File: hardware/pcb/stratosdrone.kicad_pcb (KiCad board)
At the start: 4 copper layers, 38 x 74 mm, 115 parts, among them J1 BATT_PH2, J10 DBG, J11 C6DBG, J2 USB-C-16P, J3 FLOW_HDR, J4 CAM_FFC15, J5 MOTOR1, J6 MOTOR2, J7 MOTOR3, J8 MOTOR4, J9 EXP, Q1 AO3400A, Q2 AO3400A, Q3 AO3400A, Q4 AO3400A, SW1 RESET, SW2 BOOT, U1 ESP32-P4NRW32, U10 TLV62569DBVR, U2 W25Q128JVSIQ, U3 ESP32-C6-MINI-1, U4 TP4056-42-ESOP8, U5 SY8089AAAC, U6 ICM-42688-P, U7 SPL06-001, U8 VL53L1X, U9 PMW3901MB, Y1 40MHz

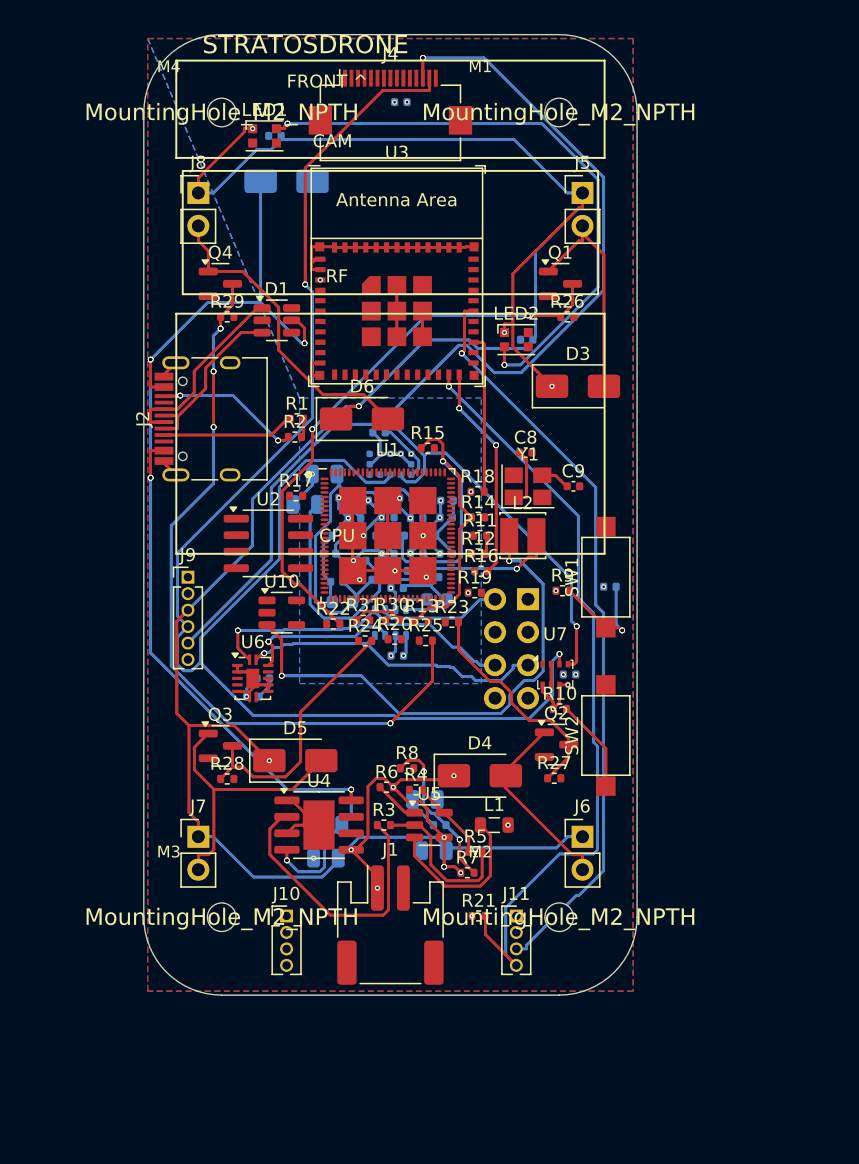
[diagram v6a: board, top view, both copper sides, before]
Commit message: pcb: add 51 clearance-checked power stitch vias; document the true routing gap
Verification pass on the PCB (placement, routing, sensors, camera):

- Ran connect_power() (pure pcbnew, no autorouter) to stitch power-net pads
  not already touching their plane: +51 clearance-checked vias (172 total,
  up from 121). Re-exported gerbers + the JLCPCB zip.
- Confirmed with KiCad's own connectivity engine (not eyeballing): 106
  pad-pairs across 73 nets are still ratsnest, almost all needing just one
  more short trace/via. Full net list now in KNOWN_GAPS.md item 1.
- Verified sensor + camera placement against the frame: the ToF/flow Y
  offsets in body_bottom_v2.scad (tof_pos=[0,-3.9], flow_pos=[0,8.3]) match
  the PCB's board-center-relative positions exactly; camera FFC sits at the
  nose, matching the frame's front-wall opening.
- Identified the "8 holes" connector: J3 (FLOW_HDR), a DNP 2x4 fallback
  header for the optical-flow sensor — populate U9 (soldered PMW3901) OR
  J3 (external CJMCU-3901 breakout), not both.
- Tried 5 different headless-Freerouting configurations to close the
  remaining gap automatically; all 5 converge on the routing internally but
  never write the session file (looks like a real bug in Freerouting
  2.1.0's post-route save path under a headless X server, not a config
  issue — documented in KNOWN_GAPS/ROUTING so it isn't re-attempted blind).

Board is NOT yet ready to order: the zip in jlcpcb/ reflects the current,
mostly-but-not-fully-routed state. KNOWN_GAPS.md lists the fastest paths to
close the last ~106 connections (KiCad direct / DeepPCB.ai / Freerouting
with a real display).

Co-Authored-By: Claude Opus 4.8 <noreply@anthropic.com>
Claude-Session: https://claude.ai/code/session_011szEEHZ8KTTsZmGFgY6Cjw
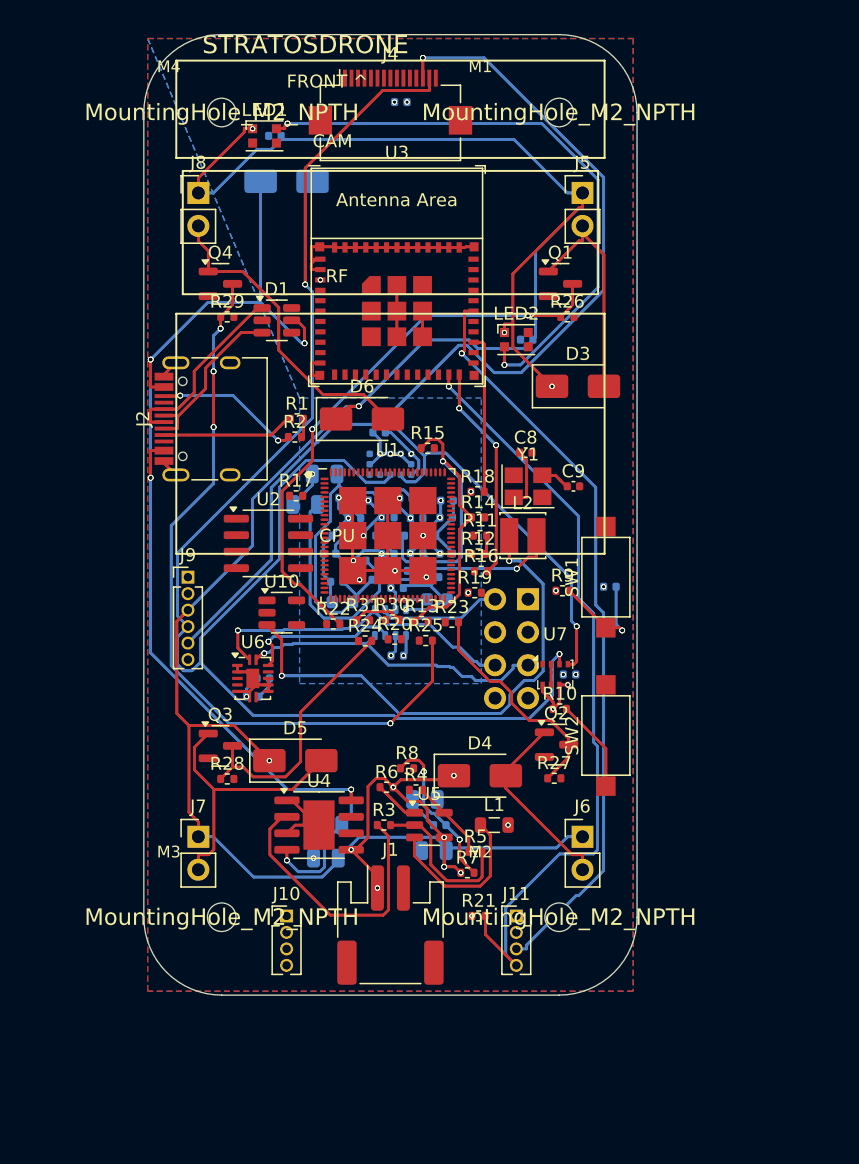
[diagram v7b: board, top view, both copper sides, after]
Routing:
- net VBAT: vias 14 -> 24
- net GND: vias 28 -> 56
- net 3V3: vias 13 -> 26
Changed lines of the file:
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@@
   (segment (start 13.55 16.35) (end 14.65 16.35) (width 0.2) (layer "F.Cu") (net 1))
   (segment (start 21.9 16.4) (end 21.1 16.4) (width 0.2) (layer "F.Cu") (net 1))
+  (via (at 21.765343 41.796811) (size 0.4) (drill 0.2) (layers "F.Cu" "B.Cu") (net 1))
   (via (at 18.32 40) (size 0.4) (drill 0.2) (layers "F.Cu" "B.Cu") (net 1))
   (via (at 19.348354 41.311547) (size 0.4) (drill 0.2) (layers "F.Cu" "B.Cu") (net 1))
   (via (at 17.291645 35.888452) (size 0.4) (drill 0.2) (layers "F.Cu" "B.Cu") (net 1))
+  (via (at 20.54149 39.950918) (size 0.4) (drill 0.2) (layers "F.Cu" "B.Cu") (net 1))
   (via (at 16.149318 40.523055) (size 0.4) (drill 0.2) (layers "F.Cu" "B.Cu") (net 1))
   (via (at 7.92 51) (size 0.4) (drill 0.2) (layers "F.Cu" "B.Cu") (net 1))
   (via (at 22.811192 37.21465) (size 0.4) (drill 0.2) (layers "F.Cu" "B.Cu") (net 1))
+  (via (at 7.92 51) (size 0.4) (drill 0.2) (layers "F.Cu" "B.Cu") (net 1))
   (via (at 15.752177 37.252302) (size 0.4) (drill 0.2) (layers "F.Cu" "B.Cu") (net 1))
+  (via (at 15.752177 37.252302) (size 0.4) (drill 0.2) (layers "F.Cu" "B.Cu") (net 1))
+  (via (at 12.980165 33.853979) (size 0.4) (drill 0.2) (layers "F.Cu" "B.Cu") (net 1))
   (via (at 19.32 5.2) (size 0.4) (drill 0.2) (layers "F.Cu" "B.Cu") (net 1))
+  (via (at 18.2 32.3) (size 0.4) (drill 0.2) (layers "F.Cu" "B.Cu") (net 1))
+  (via (at 19.8 32.3) (size 0.4) (drill 0.2) (layers "F.Cu" "B.Cu") (net 1))
+  (via (at 13.078985 63.445618) (size 0.4) (drill 0.2) (layers "F.Cu" "B.Cu") (net 1))
   (via (at 16.626194 42.00162) (size 0.4) (drill 0.2) (layers "F.Cu" "B.Cu") (net 1))
   (via (at 21.765343 41.796811) (size 0.4) (drill 0.2) (layers "F.Cu" "B.Cu") (net 1))
   (via (at 19 32.3) (size 0.4) (drill 0.2) (layers "F.Cu" "B.Cu") (net 1))
+  (via (at 17.291645 35.888452) (size 0.4) (drill 0.2) (layers "F.Cu" "B.Cu") (net 1))
+  (via (at 22.880128 35.899031) (size 0.4) (drill 0.2) (layers "F.Cu" "B.Cu") (net 1))
   (via (at 21.52 38.6) (size 0.4) (drill 0.2) (layers "F.Cu" "B.Cu") (net 1))
   (via (at 18.32 37.2) (size 0.4) (drill 0.2) (layers "F.Cu" "B.Cu") (net 1))
   (via (at 19.8 32.3) (size 0.4) (drill 0.2) (layers "F.Cu" "B.Cu") (net 1))
+  (via (at 19.031957 42.637711) (size 0.4) (drill 0.2) (layers "F.Cu" "B.Cu") (net 1))
+  (via (at 16.626194 42.00162) (size 0.4) (drill 0.2) (layers "F.Cu" "B.Cu") (net 1))
   (via (at 20.54149 37.249081) (size 0.4) (drill 0.2) (layers "F.Cu" "B.Cu") (net 1))
+  (via (at 19.708427 35.716899) (size 0.4) (drill 0.2) (layers "F.Cu" "B.Cu") (net 1))
+  (via (at 19.348354 41.311547) (size 0.4) (drill 0.2) (layers "F.Cu" "B.Cu") (net 1))
+  (via (at 19 32.3) (size 0.4) (drill 0.2) (layers "F.Cu" "B.Cu") (net 1))
+  (via (at 16.149318 40.523055) (size 0.4) (drill 0.2) (layers "F.Cu" "B.Cu") (net 1))
   (via (at 19.048985 47.845618) (size 0.4) (drill 0.2) (layers "F.Cu" "B.Cu") (net 1))
+  (via (at 18.32 40) (size 0.4) (drill 0.2) (layers "F.Cu" "B.Cu") (net 1))
   (via (at 15.026552 35.68226) (size 0.4) (drill 0.2) (layers "F.Cu" "B.Cu") (net 1))
+  (via (at 15.026552 35.68226) (size 0.4) (drill 0.2) (layers "F.Cu" "B.Cu") (net 1))
+  (via (at 16.92 38.6) (size 0.4) (drill 0.2) (layers "F.Cu" "B.Cu") (net 1))
   (via (at 18.2 32.3) (size 0.4) (drill 0.2) (layers "F.Cu" "B.Cu") (net 1))
   (via (at 20.54149 39.950918) (size 0.4) (drill 0.2) (layers "F.Cu" "B.Cu") (net 1))
+  (via (at 21.52 38.6) (size 0.4) (drill 0.2) (layers "F.Cu" "B.Cu") (net 1))
+  (via (at 35.426146 42.539103) (size 0.4) (drill 0.2) (layers "F.Cu" "B.Cu") (net 1))
   (via (at 19.708427 35.716899) (size 0.4) (drill 0.2) (layers "F.Cu" "B.Cu") (net 1))
+  (via (at 19.32 5.2) (size 0.4) (drill 0.2) (layers "F.Cu" "B.Cu") (net 1))
   (via (at 22.880128 35.899031) (size 0.4) (drill 0.2) (layers "F.Cu" "B.Cu") (net 1))
   (via (at 19.031957 42.637711) (size 0.4) (drill 0.2) (layers "F.Cu" "B.Cu") (net 1))
+  (via (at 32.319999 49.3) (size 0.4) (drill 0.2) (layers "F.Cu" "B.Cu") (net 1))
   (via (at 35.426146 42.539103) (size 0.4) (drill 0.2) (layers "F.Cu" "B.Cu") (net 1))
+  (via (at 20.54149 37.249081) (size 0.4) (drill 0.2) (layers "F.Cu" "B.Cu") (net 1))
+  (via (at 22.811192 39.985349) (size 0.4) (drill 0.2) (layers "F.Cu" "B.Cu") (net 1))
+  (via (at 22.811192 37.21465) (size 0.4) (drill 0.2) (layers "F.Cu" "B.Cu") (net 1))
   (via (at 22.811192 39.985349) (size 0.4) (drill 0.2) (layers "F.Cu" "B.Cu") (net 1))
   (via (at 12.980165 33.853979) (size 0.4) (drill 0.2) (layers "F.Cu" "B.Cu") (net 1))
+  (via (at 18.32 37.2) (size 0.4) (drill 0.2) (layers "F.Cu" "B.Cu") (net 1))
   (via (at 16.92 38.6) (size 0.4) (drill 0.2) (layers "F.Cu" "B.Cu") (net 1))
+  (via (at 19.048985 47.845618) (size 0.4) (drill 0.2) (layers "F.Cu" "B.Cu") (net 1))
   (via (at 13.078985 63.445618) (size 0.4) (drill 0.2) (layers "F.Cu" "B.Cu") (net 1))
   (via (at 32.319999 49.3) (size 0.4) (drill 0.2) (layers "F.Cu" "B.Cu") (net 1))
@@
   (via (at 31.539295 51.95) (size 0.4) (drill 0.2) (layers "F.Cu" "B.Cu") (net 4))
   (via (at 25.289999 67.9) (size 0.4) (drill 0.2) (layers "F.Cu" "B.Cu") (net 4))
+  (via (at 20.008985 47.845618) (size 0.4) (drill 0.2) (layers "F.Cu" "B.Cu") (net 4))
+  (via (at 32.675 50.1) (size 0.4) (drill 0.2) (layers "F.Cu" "B.Cu") (net 4))
+  (via (at 31.539295 51.95) (size 0.4) (drill 0.2) (layers "F.Cu" "B.Cu") (net 4))
+  (via (at 31.750512 42.84777) (size 0.4) (drill 0.2) (layers "F.Cu" "B.Cu") (net 4))
   (via (at 25.205583 35.214042) (size 0.4) (drill 0.2) (layers "F.Cu" "B.Cu") (net 4))
   (via (at 20.28 5.2) (size 0.4) (drill 0.2) (layers "F.Cu" "B.Cu") (net 4))
   (via (at 28.0625 60.9) (size 0.4) (drill 0.2) (layers "F.Cu" "B.Cu") (net 4))
+  (via (at 20.28 5.2) (size 0.4) (drill 0.2) (layers "F.Cu" "B.Cu") (net 4))
   (via (at 33.279999 49.3) (size 0.4) (drill 0.2) (layers "F.Cu" "B.Cu") (net 4))
   (via (at 20.008985 47.845618) (size 0.4) (drill 0.2) (layers "F.Cu" "B.Cu") (net 4))
   (via (at 24.99 43) (size 0.4) (drill 0.2) (layers "F.Cu" "B.Cu") (net 4))
+  (via (at 20.6 32.3) (size 0.4) (drill 0.2) (layers "F.Cu" "B.Cu") (net 4))
+  (via (at 25.205583 35.214042) (size 0.4) (drill 0.2) (layers "F.Cu" "B.Cu") (net 4))
   (via (at 20.2 44.3) (size 0.4) (drill 0.2) (layers "F.Cu" "B.Cu") (net 4))
   (via (at 32.675 50.1) (size 0.4) (drill 0.2) (layers "F.Cu" "B.Cu") (net 4))
+  (via (at 24.99 43) (size 0.4) (drill 0.2) (layers "F.Cu" "B.Cu") (net 4))
   (via (at 31.750512 42.84777) (size 0.4) (drill 0.2) (layers "F.Cu" "B.Cu") (net 4))
+  (via (at 28.0625 60.9) (size 0.4) (drill 0.2) (layers "F.Cu" "B.Cu") (net 4))
+  (via (at 13.6 18.9) (size 0.4) (drill 0.2) (layers "F.Cu" "B.Cu") (net 4))
   (via (at 20.6 32.3) (size 0.4) (drill 0.2) (layers "F.Cu" "B.Cu") (net 4))
+  (via (at 20.2 44.3) (size 0.4) (drill 0.2) (layers "F.Cu" "B.Cu") (net 4))
+  (via (at 25.289999 67.9) (size 0.4) (drill 0.2) (layers "F.Cu" "B.Cu") (net 4))
   (via (at 13.6 18.9) (size 0.4) (drill 0.2) (layers "F.Cu" "B.Cu") (net 4))
+  (via (at 33.279999 49.3) (size 0.4) (drill 0.2) (layers "F.Cu" "B.Cu") (net 4))
   (segment (start 22.2746 44.3) (end 20.2 44.3) (width 0.2) (layer "B.Cu") (net 4))
   (segment (start 15.9866 36.5267) (end 16.7122 37.2523) (width 0.2) (layer "B.Cu") (net 4))
@@
   (segment (start 3.4769 59.925) (end 4.2 60.6481) (width 0.2) (layer "F.Cu") (net 59))
   (segment (start 4.2 61.8) (end 4.2 60.6481) (width 0.2) (layer "F.Cu") (net 59))
+  (via (at 18 65.75) (size 0.4) (drill 0.2) (layers "F.Cu" "B.Cu") (net 59))
+  (via (at 15.975 62.805) (size 0.4) (drill 0.2) (layers "F.Cu" "B.Cu") (net 59))
   (via (at 31.450705 27.095905) (size 0.4) (drill 0.2) (layers "F.Cu" "B.Cu") (net 59))
   (via (at 19.216552 57.98226) (size 0.4) (drill 0.2) (layers "F.Cu" "B.Cu") (net 59))
@@
   (via (at 16.5652 28.6318) (size 0.45) (drill 0.25) (layers "F.Cu" "B.Cu") (net 59))
   (via (at 23.1375 64.1168) (size 0.45) (drill 0.25) (layers "F.Cu" "B.Cu") (net 59))
+  (via (at 31.450705 27.095905) (size 0.4) (drill 0.2) (layers "F.Cu" "B.Cu") (net 59))
   (via (at 8.385 7.25) (size 0.4) (drill 0.2) (layers "F.Cu" "B.Cu") (net 59))
   (via (at 23.891959 57.098628) (size 0.4) (drill 0.2) (layers "F.Cu" "B.Cu") (net 59))
+  (via (at 19.216552 57.98226) (size 0.4) (drill 0.2) (layers "F.Cu" "B.Cu") (net 59))
+  (via (at 24.420402 64.574607) (size 0.4) (drill 0.2) (layers "F.Cu" "B.Cu") (net 59))
+  (via (at 27.785 22.95) (size 0.4) (drill 0.2) (layers "F.Cu" "B.Cu") (net 59))
   (via (at 9.674076 55.935856) (size 0.4) (drill 0.2) (layers "F.Cu" "B.Cu") (net 59))
+  (via (at 23.891959 57.098628) (size 0.4) (drill 0.2) (layers "F.Cu" "B.Cu") (net 59))
   (via (at 16.5652 28.6318) (size 0.45) (drill 0.25) (layers "F.Cu" "B.Cu") (net 59))
   (via (at 23.1375 64.1168) (size 0.45) (drill 0.25) (layers "F.Cu" "B.Cu") (net 59))
+  (via (at 23.1375 61.85) (size 0.4) (drill 0.2) (layers "F.Cu" "B.Cu") (net 59))
   (via (at 18 65.75) (size 0.4) (drill 0.2) (layers "F.Cu" "B.Cu") (net 59))
+  (via (at 9.674076 55.935856) (size 0.4) (drill 0.2) (layers "F.Cu" "B.Cu") (net 59))
+  (via (at 8.385 7.25) (size 0.4) (drill 0.2) (layers "F.Cu" "B.Cu") (net 59))
   (segment (start 23.2973 62.6616) (end 22.4669 61.8312) (width 0.2) (layer "B.Cu") (net 59))
   (segment (start 14.979 63.6619) (end 14.979 63.4456) (width 0.2) (layer "B.Cu") (net 59))

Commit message: hardware/pcb: add Stratos Drones S-propeller logo + wordmark to silkscreen
Recreated the "S made of two swept propeller blades around a hub" logo and
the "STRATOS DRONES" wordmark on the back silkscreen (B.SilkS), matching the
project branding. Added via scripts/add_logo.py — a text-level append that
preserves the existing routing (1384 tracks / 174 vias unchanged) and is
idempotent. The mark sits in the clean B.Cu-pour area above the sensor
aperture (y<27 mm) so it never overlaps the optical windows; the wordmark
runs along the bottom edge. Documented in KNOWN_GAPS process notes; preview
render in preview/back_silk_logo.png.

Co-Authored-By: Claude Fable 5 <noreply@anthropic.com>
Claude-Session: https://claude.ai/code/session_011szEEHZ8KTTsZmGFgY6Cjw
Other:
- board text added: "STRATOS DRONES"
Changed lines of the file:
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@@
     )
   )
+  (gr_poly (pts (xy 19.125 22.000) (xy 18.921 21.828) (xy 18.727 21.644) (xy 18.543 21.451) (xy 18.368 21.248) (xy 18.204 21.035) (xy 18.051 20.815) (xy 17.908 20.587) (xy 17.777 20.351) (xy 17.656 20.109) (xy 17.547 19.862) (xy 17.451 19.609) (xy 17.366 19.352) (xy 17.293 19.091) (xy 17.233 18.826) (xy 17.186 18.560) (xy 17.152 18.291) (xy 17.132 18.021) (xy 17.125 17.750) (xy 16.946 17.926) (xy 16.783 18.118) (xy 16.637 18.326) (xy 16.509 18.548) (xy 16.398 18.783) (xy 16.306 19.028) (xy 16.232 19.282) (xy 16.176 19.544) (xy 16.141 19.812) (xy 16.124 20.085) (xy 16.128 20.361) (xy 16.153 20.639) (xy 16.198 20.916) (xy 16.264 21.192) (xy 16.352 21.465) (xy 16.462 21.734) (xy 16.595 21.996) (xy 16.750 22.250) (xy 16.815 22.331) (xy 16.884 22.407) (xy 16.958 22.479) (xy 17.036 22.545) (xy 17.118 22.606) (xy 17.204 22.662) (xy 17.294 22.713) (xy 17.387 22.758) (xy 17.484 22.797) (xy 17.585 22.830) (xy 17.689 22.858) (xy 17.796 22.880) (xy 17.907 22.895) (xy 18.020 22.904) (xy 18.136 22.907) (xy 18.255 22.903) (xy 18.376 22.892) (xy 18.500 22.875) (xy 18.581 22.853) (xy 18.657 22.829) (xy 18.729 22.802) (xy 18.795 22.772) (xy 18.856 22.739) (xy 18.912 22.704) (xy 18.963 22.665) (xy 19.008 22.623) (xy 19.047 22.578) (xy 19.080 22.529) (xy 19.108 22.477) (xy 19.130 22.421) (xy 19.145 22.361) (xy 19.154 22.298) (xy 19.157 22.230) (xy 19.153 22.158) (xy 19.142 22.081) (xy 19.125 22.000)) (stroke (width 0) (type solid)) (fill solid) (layer "B.SilkS") (tstamp stratos-logo-ed339a43-24d2-4dee-8aad-c41e2fa42c7e))
+  (gr_poly (pts (xy 18.875 23.000) (xy 19.079 23.172) (xy 19.273 23.356) (xy 19.457 23.549) (xy 19.632 23.752) (xy 19.796 23.965) (xy 19.949 24.185) (xy 20.092 24.413) (xy 20.223 24.649) (xy 20.344 24.891) (xy 20.453 25.138) (xy 20.549 25.391) (xy 20.634 25.648) (xy 20.707 25.909) (xy 20.767 26.174) (xy 20.814 26.440) (xy 20.848 26.709) (xy 20.868 26.979) (xy 20.875 27.250) (xy 21.054 27.074) (xy 21.217 26.882) (xy 21.363 26.674) (xy 21.491 26.452) (xy 21.602 26.217) (xy 21.694 25.972) (xy 21.768 25.718) (xy 21.824 25.456) (xy 21.859 25.188) (xy 21.876 24.915) (xy 21.872 24.639) (xy 21.847 24.361) (xy 21.802 24.084) (xy 21.736 23.808) (xy 21.648 23.535) (xy 21.538 23.266) (xy 21.405 23.004) (xy 21.250 22.750) (xy 21.185 22.669) (xy 21.116 22.593) (xy 21.042 22.521) (xy 20.964 22.455) (xy 20.882 22.394) (xy 20.796 22.338) (xy 20.706 22.287) (xy 20.613 22.242) (xy 20.516 22.203) (xy 20.415 22.170) (xy 20.311 22.142) (xy 20.204 22.120) (xy 20.093 22.105) (xy 19.980 22.096) (xy 19.864 22.093) (xy 19.745 22.097) (xy 19.624 22.108) (xy 19.500 22.125) (xy 19.419 22.147) (xy 19.343 22.171) (xy 19.271 22.198) (xy 19.205 22.228) (xy 19.144 22.261) (xy 19.088 22.296) (xy 19.037 22.335) (xy 18.992 22.377) (xy 18.953 22.422) (xy 18.920 22.471) (xy 18.892 22.523) (xy 18.870 22.579) (xy 18.855 22.639) (xy 18.846 22.702) (xy 18.843 22.770) (xy 18.847 22.842) (xy 18.858 22.919) (xy 18.875 23.000)) (stroke (width 0) (type solid)) (fill solid) (layer "B.SilkS") (tstamp stratos-logo-5fa175e6-d708-49c5-ba64-9c1fbd1f2083))
+  (gr_circle (center 19.000 22.500) (end 19.938 22.500) (stroke (width 0.625) (type solid)) (fill none) (layer "B.SilkS") (tstamp stratos-logo-dd315498-a2ae-4508-9006-7bf8bd8fba50))
+  (gr_circle (center 19.000 22.500) (end 19.250 22.500) (stroke (width 0.000) (type solid)) (fill solid) (layer "B.SilkS") (tstamp stratos-logo-91948ab8-85fd-444a-baa2-42ef5cbcf667))
+  (gr_text "STRATOS DRONES" (at 19.000 68.500) (layer "B.SilkS") (effects (font (size 1.5 1.5) (thickness 0.24)) (justify mirror)) (tstamp stratos-logo-23bec2c9-b6ea-45ba-b376-d6d8769c42ab))
 )
